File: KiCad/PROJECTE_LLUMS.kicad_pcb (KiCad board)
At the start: 2 copper layers, 116.3 x 86.1 mm, 70 parts, among them J1 CONNECTOR_MOTOR, J10 Conn_01x02_Pin, J2 DE9_Pins_MountingHoles, J3 Conn_01x05, J4 Conn_01x02_Pin, J5 DE9_Pins_MountingHoles, J6 Conn_01x02_Pin, J7 Conn_01x02_Pin, J8 Conn_01x02_Pin, J9 Conn_01x02_Pin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

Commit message: errors 3V3
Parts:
- moved R19 0.25 mm to (131.2, 104.5), turned to 0 degrees
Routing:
- net +3V3: track 34.6 -> 44.1 mm, vias 31 -> 35
- net (no net): track 8.60 -> 3.50 mm, vias 4 -> 2
- net I2C_SCL: track 37.1 -> 39.7 mm
- net CARRETERA: track 127.0 -> 129.0 mm
- net I2C_SDA: track 41.3 -> 42.2 mm
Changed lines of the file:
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@@
 	(footprint "Resistor_SMD:R_0805_2012Metric_Pad1.20x1.40mm_HandSolder"
 		(layer "F.Cu")
-		(at 131.5 104.5 180)
+		(at 131.25 104.5)
 		(descr "Resistor SMD 0805 (2012 Metric), square (rectangular) end terminal, IPC-7351 nominal with elongated pad for handsoldering. (Body size source: IPC-SM-782 page 72, https://www.pcb-3d.com/wordpress/wp-content/uploads/ipc-sm-782a_amendment_1_and_2.pdf), generated with kicad-footprint-generator")
 		(tags "resistor handsolder")
 		(property "Reference" "R19"
-			(at 0 -1.65 0)
+			(at 0 1.7 0)
 			(layer "F.SilkS")
 			(effects
@@
 		)
 		(property "Value" "4.7k"
-			(at 0 -3.1 0)
+			(at 0 3 0)
 			(layer "F.Fab")
 			(effects
@@
 		(attr smd)
 		(fp_line
-			(start -0.227064 0.735)
-			(end 0.227064 0.735)
+			(start -0.227064 -0.735)
+			(end 0.227064 -0.735)
 			(stroke
 				(width 0.12)
@@
 		)
 		(fp_line
-			(start -0.227064 -0.735)
-			(end 0.227064 -0.735)
+			(start -0.227064 0.735)
+			(end 0.227064 0.735)
 			(stroke
 				(width 0.12)
@@
 		)
 		(pad "1" smd roundrect
-			(at -1 0 180)
+			(at -1 0)
 			(size 1.2 1.4)
 			(layers "F.Cu" "F.Mask" "F.Paste")
@@
 		)
 		(pad "2" smd roundrect
-			(at 1 0 180)
+			(at 1 0)
 			(size 1.2 1.4)
 			(layers "F.Cu" "F.Mask" "F.Paste")
@@
 	)
 	(via
-		(at 171.2 68.8)
-		(size 0.6)
-		(drill 0.3)
-		(layers "F.Cu" "B.Cu")
-		(net 0)
-	)
-	(via
-		(at 171.2 74)
-		(size 0.6)
-		(drill 0.3)
-		(layers "F.Cu" "B.Cu")
-		(net 0)
-	)
-	(via
 		(at 156.1 95.1)
 		(size 0.6)
@@
 	)
 	(segment
-		(start 171.2 68.9)
-		(end 171.2 74)
-		(width 0.2)
-		(layer "B.Cu")
-		(net 0)
-	)
-	(segment
 		(start 152.6 95.1)
 		(end 156.1 95.1)
@@
 	)
 	(segment
-		(start 130 104)
-		(end 130.5 104.5)
-		(width 0.2)
-		(layer "F.Cu")
-		(net 1)
-	)
-	(segment
 		(start 125.2 103.1)
 		(end 125.5 103.4)
@@
 	)
 	(via
+		(at 171.2 68.8)
+		(size 0.6)
+		(drill 0.3)
+		(layers "F.Cu" "B.Cu")
+		(net 1)
+	)
+	(via
 		(at 146.4 81.6)
 		(size 0.6)
@@
 	)
 	(via
+		(at 170 102.75)
+		(size 0.6)
+		(drill 0.3)
+		(layers "F.Cu" "B.Cu")
+		(free yes)
+		(net 1)
+	)
+	(via
 		(at 165.6 94.6)
 		(size 0.6)
@@
 	)
 	(via
+		(at 170 97.55)
+		(size 0.6)
+		(drill 0.3)
+		(layers "F.Cu" "B.Cu")
+		(net 1)
+	)
+	(via
 		(at 147.5 100.3)
 		(size 0.6)
@@
 	)
 	(via
+		(at 171.2 74)
+		(size 0.6)
+		(drill 0.3)
+		(layers "F.Cu" "B.Cu")
+		(free yes)
+		(net 1)
+	)
+	(via
 		(at 165.6 87.2)
 		(size 0.6)
@@
 	)
 	(segment
+		(start 171.2 68.9)
+		(end 171.2 74)
+		(width 0.2)
+		(layer "B.Cu")
+		(net 1)
+	)
+	(segment
 		(start 165.6 95.8)
 		(end 165.6 94.6)
@@
 	)
 	(segment
+		(start 170 97.65)
+		(end 170 102.75)
+		(width 0.2)
+		(layer "B.Cu")
+		(net 1)
+	)
+	(segment
 		(start 165.8 81.1)
 		(end 164.4 81.1)
@@
 	)
 	(segment
-		(start 128 106.2)
-		(end 128.3 105.9)
+		(start 133.7 107.3)
+		(end 127.9 107.3)
 		(width 0.2)
 		(layer "F.Cu")
@@
 	)
 	(segment
-		(start 142.3 97.1)
-		(end 132.1 107.3)
+		(start 137.81 84.51)
+		(end 142.3 89)
 		(width 0.2)
 		(layer "F.Cu")
@@
 	(segment
 		(start 142.3 89)
-		(end 142.3 97.1)
+		(end 142.3 98.7)
 		(width 0.2)
 		(layer "F.Cu")
@@
 	)
 	(segment
-		(start 128.3 105.9)
-		(end 128.3 105)
+		(start 128 106.2)
+		(end 128.3 105.9)
 		(width 0.2)
 		(layer "F.Cu")
@@
 	)
 	(segment
-		(start 136.3275 84.51)
-		(end 137.81 84.51)
+		(start 142.3 98.7)
+		(end 133.7 107.3)
 		(width 0.2)
 		(layer "F.Cu")
@@
 	)
 	(segment
-		(start 137.81 84.51)
-		(end 142.3 89)
+		(start 128.3 105.9)
+		(end 128.3 105)
 		(width 0.2)
 		(layer "F.Cu")
@@
 	)
 	(segment
-		(start 132.1 107.3)
-		(end 127.9 107.3)
+		(start 136.3275 84.51)
+		(end 137.81 84.51)
 		(width 0.2)
 		(layer "F.Cu")
@@
 	)
 	(segment
-		(start 194.35 48.25)
-		(end 191.4 51.2)
-		(width 0.2)
-		(layer "B.Cu")
-		(net 13)
-	)
-	(segment
-		(start 180.5 56.9)
-		(end 180.5 91.4)
+		(start 186.2 51.2)
+		(end 180.5 56.9)
 		(width 0.2)
 		(layer "B.Cu")
@@
 	)
 	(segment
-		(start 186.2 51.2)
-		(end 180.5 56.9)
+		(start 191.4 51.2)
+		(end 186.2 51.2)
 		(width 0.2)
 		(layer "B.Cu")
@@
 	)
 	(segment
-		(start 180.5 91.4)
-		(end 166.95 104.95)
+		(start 162.3 106.7)
+		(end 164.05 104.95)
 		(width 0.2)
 		(layer "B.Cu")
@@
 	)
 	(segment
-		(start 191.4 51.2)
-		(end 186.2 51.2)
+		(start 180.5 56.9)
+		(end 180.5 94.75)
 		(width 0.2)
 		(layer "B.Cu")
@@
 	)
 	(segment
-		(start 162.3 106.7)
-		(end 164.05 104.95)
+		(start 170.3 104.95)
+		(end 165.5 104.95)
 		(width 0.2)
 		(layer "B.Cu")
@@
 	)
 	(segment
-		(start 166.95 104.95)
-		(end 165.5 104.95)
+		(start 180.5 94.75)
+		(end 170.3 104.95)
 		(width 0.2)
 		(layer "B.Cu")
@@
 	)
 	(segment
+		(start 194.35 48.25)
+		(end 191.4 51.2)
+		(width 0.2)
+		(layer "B.Cu")
+		(net 13)
+	)
+	(segment
 		(start 164.05 104.95)
 		(end 165.5 104.95)
@@
 	)
 	(segment
-		(start 130.1 103.4)
-		(end 130.7 102.8)
+		(start 128.9 102.1)
+		(end 129.4 101.6)
 		(width 0.2)
 		(layer "F.Cu")
@@
 	)
 	(segment
-		(start 138.18 85.78)
-		(end 136.3275 85.78)
-		(width 0.2)
-		(layer "F.Cu")
-		(net 26)
-	)
-	(segment
-		(start 130.7 102.8)
+		(start 129.4 101.6)
 		(end 130.7 101.6)
 		(width 0.2)
@@
 	)
 	(segment
-		(start 128.3 104)
-		(end 128.802 104)
+		(start 128.9 103.4)
+		(end 128.9 102.1)
 		(width 0.2)
 		(layer "F.Cu")
@@
 	)
 	(segment
-		(start 132.5 105.3)
-		(end 132.5 104.5)
+		(start 141.4 89)
+		(end 141.4 98.6)
 		(width 0.2)
 		(layer "F.Cu")
@@
 	)
 	(segment
-		(start 129.9 105.9)
-		(end 131.9 105.9)
+		(start 136.3275 85.78)
+		(end 138.18 85.78)
 		(width 0.2)
 		(layer "F.Cu")
@@
 	)
 	(segment
-		(start 141.4 97.1)
-		(end 141.4 89)
+		(start 130.25 104.5)
+		(end 130.25 103.5)
 		(width 0.2)
 		(layer "F.Cu")
@@
 	)
 	(segment
-		(start 128.802 104)
-		(end 129.3 104.498)
+		(start 130.7 103.05)
+		(end 130.7 101.6)
 		(width 0.2)
 		(layer "F.Cu")
@@
 	)
 	(segment
-		(start 129.3 104.498)
-		(end 129.3 105.3)
+		(start 141.4 98.6)
+		(end 133.75 106.25)
 		(width 0.2)
 		(layer "F.Cu")
@@
 	)
 	(segment
-		(start 131.9 105.9)
-		(end 132.5 105.3)
+		(start 128.3 104)
+		(end 128.9 103.4)
 		(width 0.2)
 		(layer "F.Cu")
@@
 	)
 	(segment
-		(start 134 104.5)
-		(end 141.4 97.1)
+		(start 138.18 85.78)
+		(end 141.4 89)
 		(width 0.2)
 		(layer "F.Cu")
@@
 	)
 	(segment
-		(start 141.4 89)
-		(end 138.18 85.78)
+		(start 130.25 105.75)
+		(end 130.25 104.5)
 		(width 0.2)
 		(layer "F.Cu")
@@
 	)
 	(segment
-		(start 128.3 104)
-		(end 128.9 103.4)
+		(start 130.75 106.25)
+		(end 130.25 105.75)
 		(width 0.2)
 		(layer "F.Cu")
@@
 	)
 	(segment
-		(start 132.5 104.5)
-		(end 134 104.5)
+		(start 133.75 106.25)
+		(end 130.75 106.25)
 		(width 0.2)
 		(layer "F.Cu")
@@
 	)
 	(segment
-		(start 128.9 103.4)
-		(end 130.1 103.4)
+		(start 130.25 103.5)
+		(end 130.7 103.05)
 		(width 0.2)
 		(layer "F.Cu")
@@
 	)
 	(segment
-		(start 129.3 105.3)
-		(end 129.9 105.9)
+		(start 130 104)
+		(end 130.5 104.5)
 		(width 0.2)
 		(layer "F.Cu")

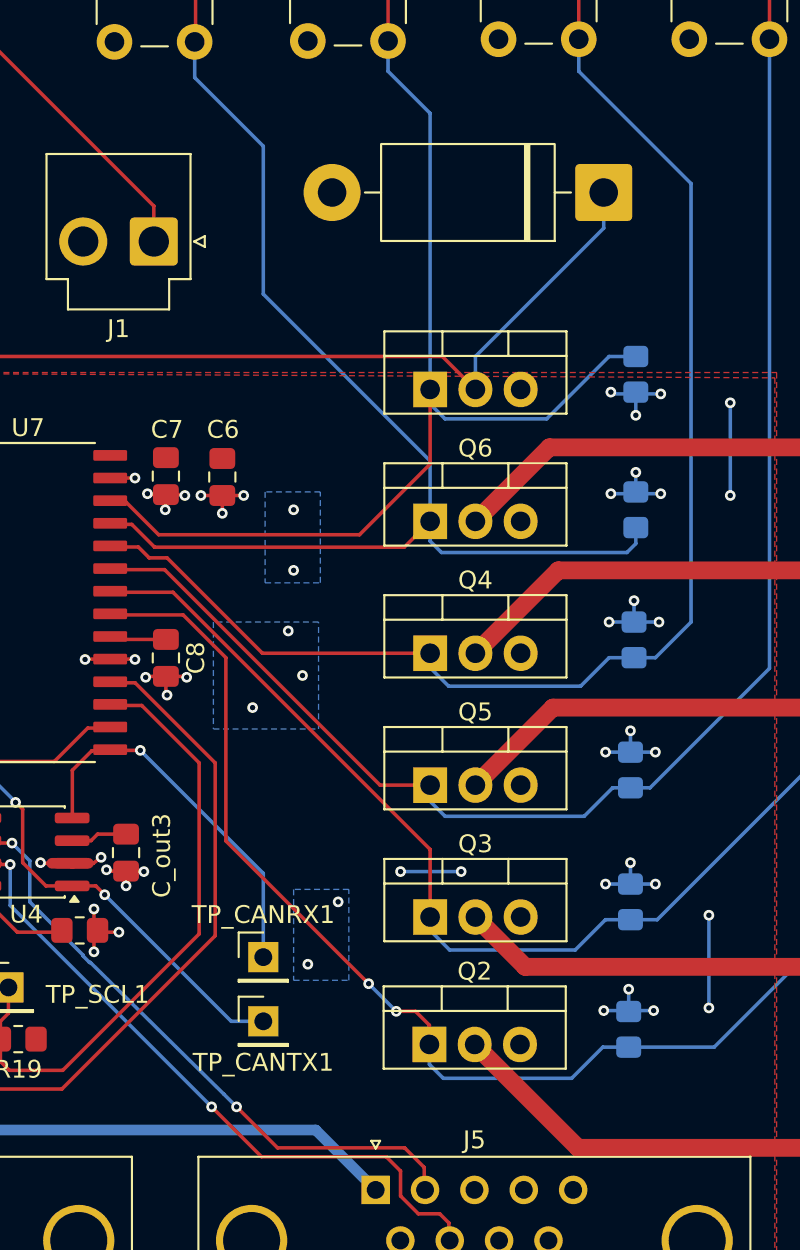
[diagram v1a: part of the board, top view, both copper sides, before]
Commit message: LLums finals amb resistències afegides
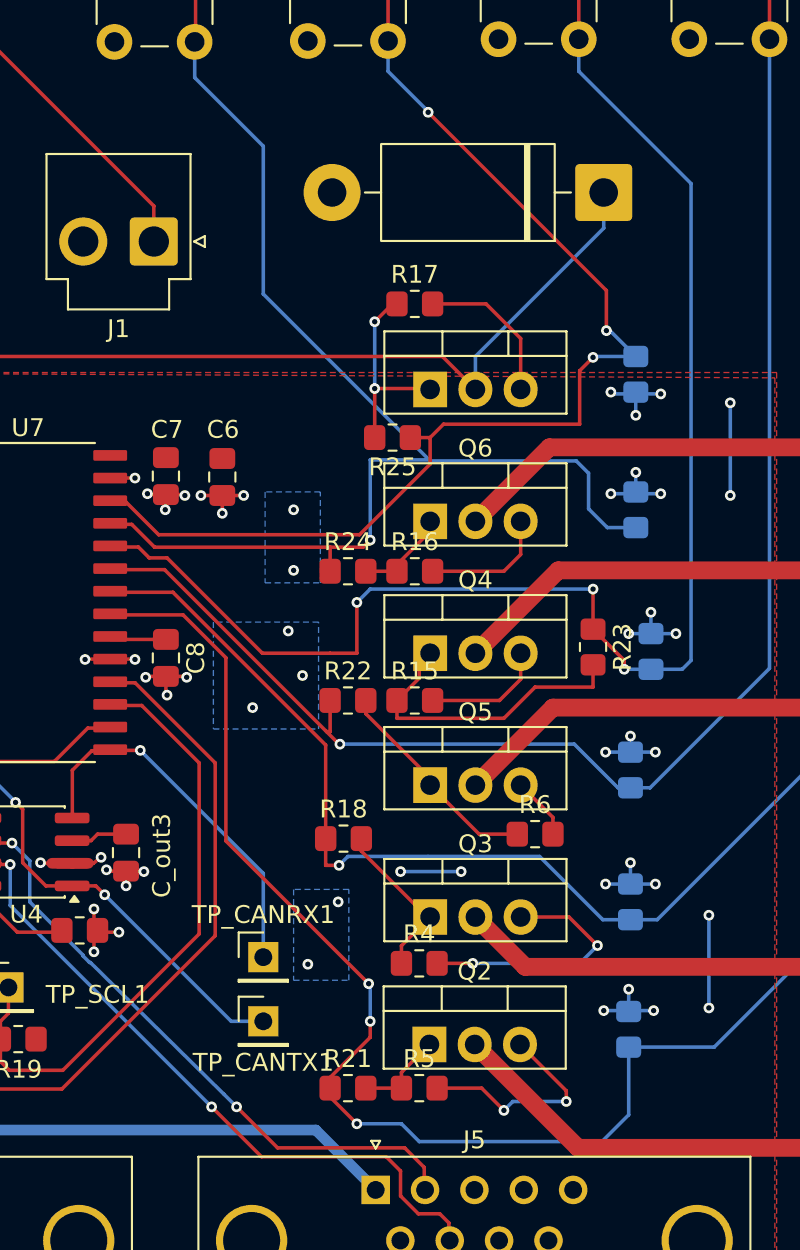
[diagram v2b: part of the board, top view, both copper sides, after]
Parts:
- added R15: 10k, Resistor_SMD:R_0805_2012Metric_Pad1.20x1.40mm_HandSolder, F.Cu at (153.5, 85.5)
- added R16: 10k, Resistor_SMD:R_0805_2012Metric_Pad1.20x1.40mm_HandSolder, F.Cu at (153.5, 78.2)
- added R17: 10k, Resistor_SMD:R_0805_2012Metric_Pad1.20x1.40mm_HandSolder, F.Cu at (153.5, 63.2)
- added R18: 220, Resistor_SMD:R_0805_2012Metric_Pad1.20x1.40mm_HandSolder, F.Cu at (149.5, 93.2)
- added R21: 220, Resistor_SMD:R_0805_2012Metric_Pad1.20x1.40mm_HandSolder, F.Cu at (149.8, 107.2)
- added R22: 220, Resistor_SMD:R_0805_2012Metric_Pad1.20x1.40mm_HandSolder, F.Cu at (149.8, 85.5)
- added R23: 220, Resistor_SMD:R_0805_2012Metric_Pad1.20x1.40mm_HandSolder, F.Cu at (163.5, 82.5)
- added R24: 220, Resistor_SMD:R_0805_2012Metric_Pad1.20x1.40mm_HandSolder, F.Cu at (149.8, 78.2)
- added R25: 220, Resistor_SMD:R_0805_2012Metric_Pad1.20x1.40mm_HandSolder, F.Cu at (152.2, 70.8)
- added R4: 10k, Resistor_SMD:R_0805_2012Metric_Pad1.20x1.40mm_HandSolder, F.Cu at (153.8, 100.2)
- added R5: 10k, Resistor_SMD:R_0805_2012Metric_Pad1.20x1.40mm_HandSolder, F.Cu at (153.8, 107.2)
- added R6: 10k, Resistor_SMD:R_0805_2012Metric_Pad1.20x1.40mm_HandSolder, F.Cu at (160.2, 93.0)
- moved R12 1.15 mm to (166.8, 82.8)
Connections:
- Q2 pad 1: CARRETERA -> Net-(Q2-G)
- Q3 pad 1: ENCREUAMENT -> Net-(Q3-G)
- Q4 pad 1: INTERM. ESQ -> Net-(Q4-G)
- Q5 pad 1: DIURNA -> Net-(Q5-G)
- Q6 pad 1: INTERM. DRT -> Net-(Q6-G)
- Q7 pad 1: NETEJA-FARS -> Net-(Q7-G)
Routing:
- net GND: track 66.4 -> 119.2 mm, vias 52 -> 56
- net Net-(Q4-G): track 0.00 -> 18.0 mm
- net Net-(Q5-G): track 0.00 -> 12.4 mm
- net Net-(Q7-G): track 0.00 -> 10.9 mm, vias 0 -> 2
- net CARRETERA: track 129.0 -> 139.7 mm, vias 2 -> 3
- net Net-(Q3-G): track 0.00 -> 9.45 mm
- net INTERM. ESQ: track 79.7 -> 85.9 mm, vias 0 -> 3
- net Net-(Q6-G): track 0.00 -> 5.15 mm
- net Net-(Q2-G): track 0.00 -> 4.70 mm
- net NETEJA-FARS: track 65.8 -> 68.5 mm, vias 0 -> 3
- net INTERM. DRT: track 72.1 -> 74.3 mm, vias 0 -> 1
- net ENCREUAMENT: track 105.4 -> 105.7 mm, vias 0 -> 1
- net DIURNA: track 88.6 -> 88.7 mm, vias 0 -> 1

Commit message: errors finals
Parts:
- moved R23 15.2 mm to (148.3, 82.9)
- moved R6 10.0 mm to (150.5, 90.6), turned to -90 degrees
- moved R17 5.87 mm to (150.5, 68.3), turned to -90 degrees
- moved R22 5.30 mm to (148.3, 90.6), turned to 90 degrees
- moved R18 4.76 mm to (148.5, 97.9), turned to -90 degrees
- moved R25 4.65 mm to (148.3, 68.3), turned to 90 degrees
- moved R15 3.97 mm to (150.5, 82.9), turned to 90 degrees
- moved R16 3.94 mm to (150.5, 75.7), turned to -90 degrees
- moved R4 3.85 mm to (150.7, 97.9), turned to 90 degrees
- moved R5 3.64 mm to (150.5, 105.6), turned to -90 degrees
- moved R24 2.93 mm to (148.3, 75.7), turned to 90 degrees
- moved R21 2.20 mm to (148.3, 105.6), turned to 90 degrees
- moved Q2 2.00 mm to (155.9, 106.0)
- moved Q4 2.00 mm to (156.0, 84.0)
- moved Q5 2.00 mm to (156.0, 91.5)
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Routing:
- net GND: track 119.2 -> 84.4 mm, vias 56 -> 69
- net Net-(Q4-G): track 18.0 -> 7.72 mm
- net +3V3: track 43.7 -> 51.4 mm, vias 35 -> 34
- net ENCREUAMENT: track 105.7 -> 111.5 mm
- net CARRETERA: track 139.7 -> 134.1 mm, vias 3 -> 1
- net INTERM. DRT: track 74.3 -> 69.4 mm, vias 1 -> 2
- net DIURNA: track 88.7 -> 93.0 mm
- net INTERM. ESQ: track 85.9 -> 82.0 mm, vias 3 -> 1
- net Net-(Q5-G): track 12.4 -> 8.43 mm
- net Net-(Q2-G): track 4.70 -> 8.20 mm
- net (no net): track 3.50 -> 0.00 mm, vias 2 -> 0
- net Net-(Q6-G): track 5.15 -> 8.47 mm
- net NETEJA-FARS: track 68.5 -> 71.5 mm
- net /llums/RELÉ: track 53.6 -> 56.4 mm
- net Net-(Q7-G): track 10.9 -> 8.43 mm, vias 2 -> 0
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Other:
- board size 116.3 x 86.1 mm -> 116.1 x 86.1 mm

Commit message: push final (?)
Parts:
- INT. DRT: renamed from SW5
- INT. ESQ: renamed from SW6
- renumbered SW1 to CARRETERA, SW3 to DIURNA, SW2 to ENCREUAMENT, SW4 to FARS
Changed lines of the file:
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@@
 		(descr "Generic 6mm SW tactile push button")
 		(tags "tact sw push 6mm")
-		(property "Reference" "SW6"
+		(property "Reference" "INT. ESQ"
 			(at -3.3 2.3 0)
 			(layer "F.SilkS")
@@
 		(descr "Generic 6mm SW tactile push button")
 		(tags "tact sw push 6mm")
-		(property "Reference" "SW2"
+		(property "Reference" "ENCREUAMENT"
 			(at -3.3 2.35 0)
 			(layer "F.SilkS")
@@
 		(descr "Generic 6mm SW tactile push button")
 		(tags "tact sw push 6mm")
-		(property "Reference" "SW1"
+		(property "Reference" "CARRETERA"
 			(at -3.3 2.3 0)
 			(layer "F.SilkS")
@@
 		(descr "Generic 6mm SW tactile push button")
 		(tags "tact sw push 6mm")
-		(property "Reference" "SW4"
+		(property "Reference" "FARS"
 			(at -3.3 2.3 0)
 			(layer "F.SilkS")
@@
 		(descr "Generic 6mm SW tactile push button")
 		(tags "tact sw push 6mm")
-		(property "Reference" "SW3"
+		(property "Reference" "DIURNA"
 			(at -3.3 2.4 0)
 			(layer "F.SilkS")
@@
 		(descr "Generic 6mm SW tactile push button")
 		(tags "tact sw push 6mm")
-		(property "Reference" "SW5"
+		(property "Reference" "INT. DRT"
 			(at -3.3 2.5 0)
 			(layer "F.SilkS")
@@
 		)
 	)
+	(gr_text "12V"
+		(at 192.5 70.4 0)
+		(layer "F.SilkS")
+		(effects
+			(font
+				(size 1 1)
+				(thickness 0.2)
+				(bold yes)
+			)
+			(justify left bottom)
+		)
+	)
 	(gr_text "MCLR"
 		(at 97 109.1 90)
@@
 	)
 	(gr_text "12V"
+		(at 192.4 83.6 0)
+		(layer "F.SilkS")
+		(effects
+			(font
+				(size 1 1)
+				(thickness 0.2)
+				(bold yes)
+			)
+			(justify left bottom)
+		)
+	)
+	(gr_text "12V"
 		(at 99.5 44.25 0)
 		(layer "F.SilkS")
@@
 		)
 	)
+	(gr_text "12V"
+		(at 191.8925 109.9 0)
+		(layer "F.SilkS")
+		(effects
+			(font
+				(size 1 1)
+				(thickness 0.2)
+				(bold yes)
+			)
+			(justify left bottom)
+		)
+	)
 	(gr_text "CLK"
 		(at 107.3 108 90)
@@
 		)
 	)
+	(gr_text "12V"
+		(at 192.4 96.9 0)
+		(layer "F.SilkS")
+		(effects
+			(font
+				(size 1 1)
+				(thickness 0.2)
+				(bold yes)
+			)
+			(justify left bottom)
+		)
+	)
 	(gr_text "GND"
 		(at 102.1 108.1 90)
@@
 		(layer "F.SilkS")
 		(effects
+			(font
+				(size 1 1)
+				(thickness 0.2)
+				(bold yes)
+			)
+			(justify left bottom)
+		)
+	)
+	(gr_text "12V"
+		(at 192.5 57.5 0)
+		(layer "F.SilkS")
+		(effects

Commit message: PRESENTACIÓ FINAL
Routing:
- net +3V3: track 51.4 -> 44.7 mm, vias 34 -> 29
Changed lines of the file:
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@@
 			(outputformat 1)
 			(mirror no)
-			(drillshape 1)
+			(drillshape 0)
 			(scaleselection 1)
-			(outputdirectory "")
+			(outputdirectory "PROJECTE_LLUMS-backups/adri/")
 		)
 	)
@@
 	)
 	(segment
-		(start 127.89 88.19)
-		(end 128.7 89)
-		(width 0.2)
-		(layer "F.Cu")
-		(net 1)
-	)
-	(segment
 		(start 125.65 104.75)
 		(end 125.65 105.2)
@@
 	)
 	(segment
-		(start 103.0625 90.0375)
-		(end 101.925 88.9)
-		(width 0.2)
-		(layer "F.Cu")
-		(net 1)
-	)
-	(segment
 		(start 127.3 88.19)
 		(end 128.01 88.19)
@@
 	)
 	(segment
-		(start 112.13 83.9325)
-		(end 112.13 85.27)
-		(width 0.2)
-		(layer "F.Cu")
-		(net 1)
-	)
-	(segment
 		(start 128.7 89)
 		(end 128.8 89)
@@
 	)
 	(segment
-		(start 128.7 87.5)
-		(end 128.9 87.5)
-		(width 0.2)
-		(layer "F.Cu")
-		(net 1)
-	)
-	(segment
 		(start 125.6 104.6)
 		(end 125.65 104.75)
@@
 	)
 	(segment
-		(start 110.8325 83.9325)
-		(end 110.8 83.9)
-		(width 0.2)
-		(layer "F.Cu")
-		(net 1)
-	)
-	(segment
-		(start 112.13 85.27)
-		(end 112.1 85.3)
-		(width 0.2)
-		(layer "F.Cu")
-		(net 1)
-	)
-	(segment
-		(start 112.13 83.9325)
-		(end 110.8325 83.9325)
-		(width 0.2)
-		(layer "F.Cu")
-		(net 1)
-	)
-	(segment
-		(start 128.01 88.19)
-		(end 128.7 87.5)
-		(width 0.2)
-		(layer "F.Cu")
-		(net 1)
-	)
-	(segment
 		(start 127.3 88.19)
 		(end 127.89 88.19)
@@
 	)
 	(via
-		(at 112.1 85.3)
-		(size 0.6)
-		(drill 0.3)
-		(layers "F.Cu" "B.Cu")
-		(net 1)
-	)
-	(via
 		(at 170.2 88.6)
 		(size 0.6)
@@
 	)
 	(via
-		(at 110.8 83.9)
-		(size 0.6)
-		(drill 0.3)
-		(layers "F.Cu" "B.Cu")
-		(net 1)
-	)
-	(via
 		(at 166 73.9)
 		(size 0.6)
@@
 	)
 	(via
-		(at 128.8 89)
-		(size 0.6)
-		(drill 0.3)
-		(layers "F.Cu" "B.Cu")
-		(net 1)
-	)
-	(via
 		(at 165.6 102.9)
 		(size 0.6)
@@
 	)
 	(via
-		(at 128.9 87.5)
-		(size 0.6)
-		(drill 0.3)
-		(layers "F.Cu" "B.Cu")
-		(net 1)
-	)
-	(via
 		(at 169.6 108.2)
 		(size 0.6)
@@
 	)
 	(via
-		(at 103.0625 90.0375)
-		(size 0.6)
-		(drill 0.3)
-		(layers "F.Cu" "B.Cu")
-		(net 1)
-	)
-	(via
 		(at 171.8 84.7)
 		(size 0.6)
@@
 		(hatch edge 0.5)
 		(priority 3)
-		(connect_pads
+		(connect_pads yes
 			(clearance 0.5)
 		)
